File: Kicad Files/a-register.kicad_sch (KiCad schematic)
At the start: 20 parts

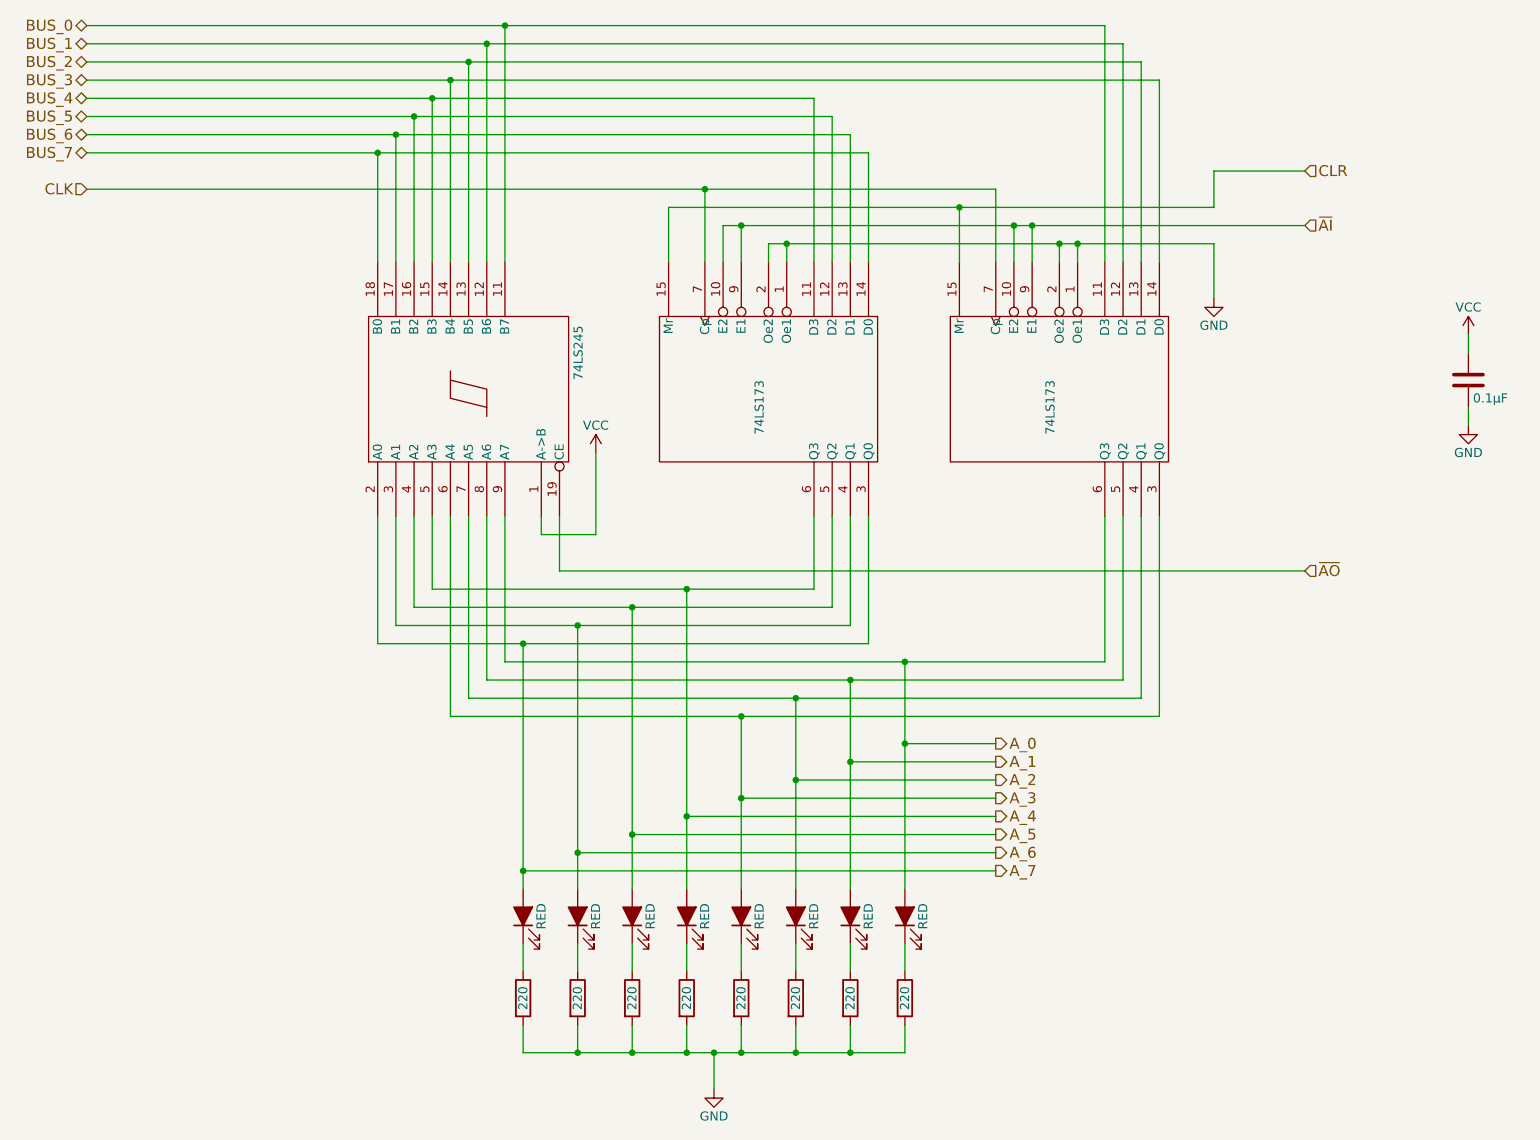
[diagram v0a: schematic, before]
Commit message: started tidy up in control
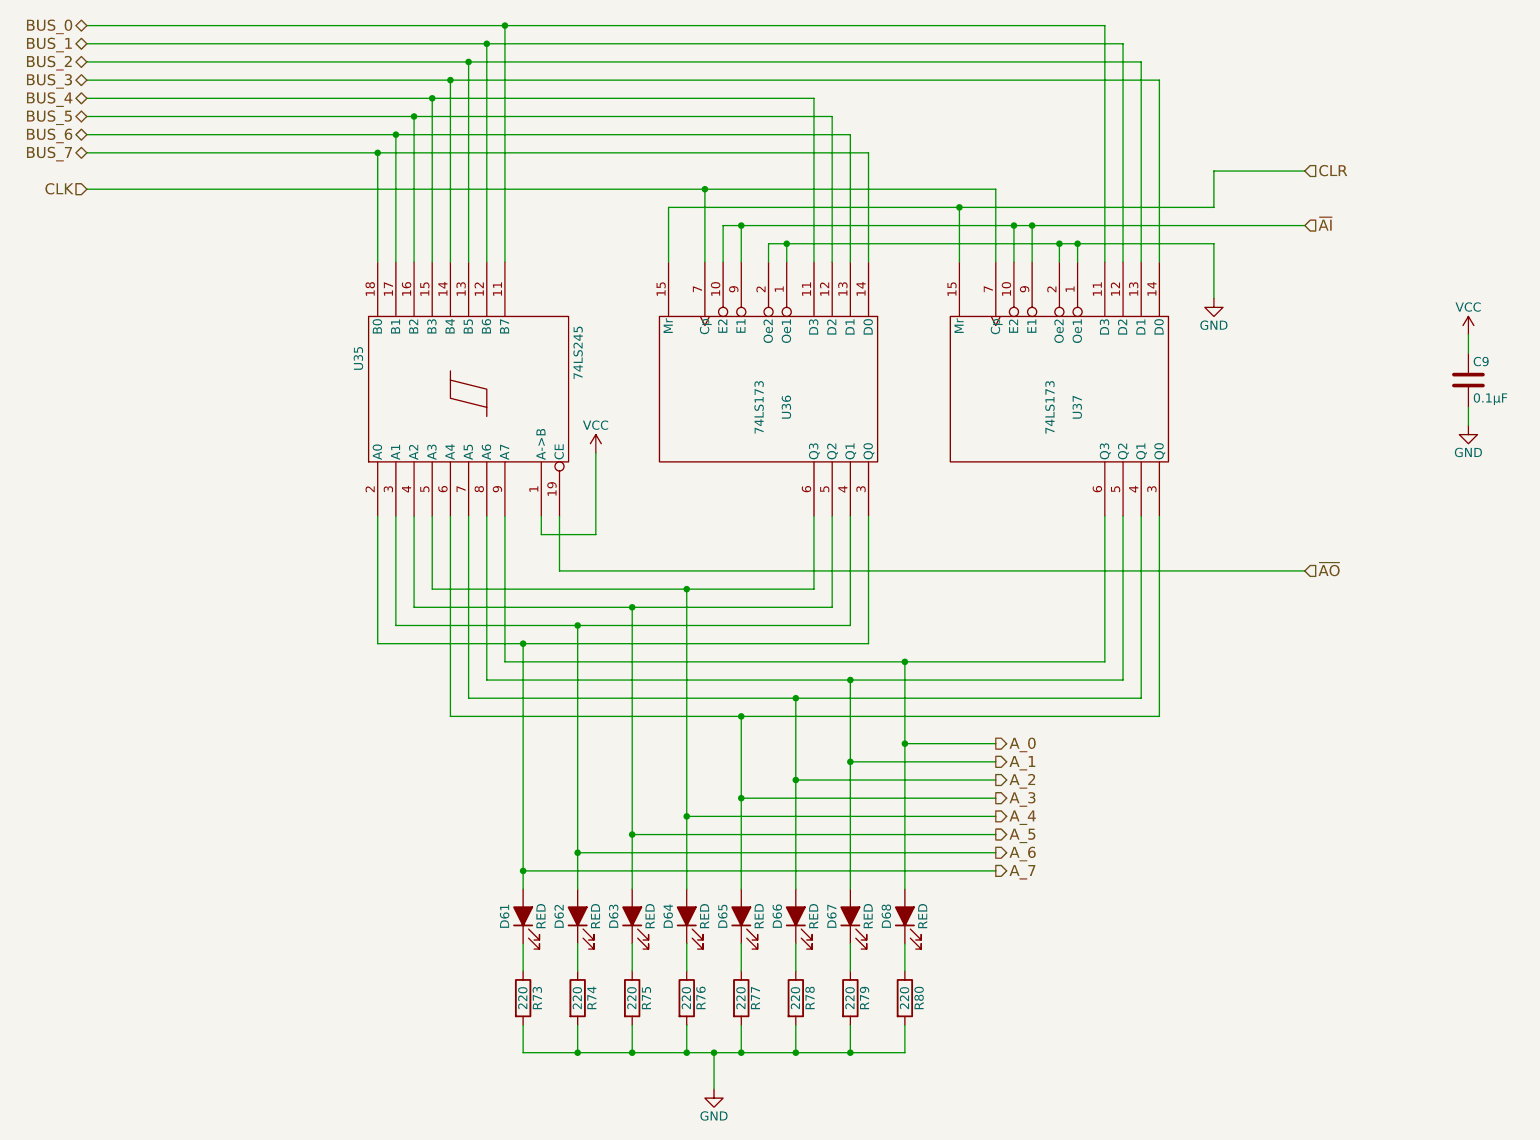
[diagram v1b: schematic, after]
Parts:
- gave numbers to parts that had none: 20
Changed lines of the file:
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@@
   (symbol (lib_id "8bit-computer-rescue:74LS173-8bit-computer-rescue") (at 133.35 68.58 270) (unit 1)
     (in_bom yes) (on_board yes)
-    (property "Reference" "" (id 0) (at 135.89 71.12 0))
+    (property "Reference" "U36" (id 0) (at 135.89 71.12 0))
     (property "Value" "74LS173" (id 1) (at 132.08 71.12 0))
     (property "Footprint" "Package_DIP:DIP-16_W7.62mm" (id 2) (at 133.35 68.58 0)
@@
   (symbol (lib_id "8bit-computer-rescue:LED_ALT-Device") (at 114.3 142.24 90) (unit 1)
     (in_bom yes) (on_board yes)
-    (property "Reference" "" (id 0) (at 111.76 142.24 0))
+    (property "Reference" "D63" (id 0) (at 111.76 142.24 0))
     (property "Value" "RED" (id 1) (at 116.84 142.24 0))
     (property "Footprint" "LED_THT:LED_D5.0mm" (id 2) (at 114.3 142.24 0)
@@
   (symbol (lib_id "8bit-computer-rescue:LED_ALT-Device") (at 144.78 142.24 90) (unit 1)
     (in_bom yes) (on_board yes)
-    (property "Reference" "" (id 0) (at 142.24 142.24 0))
+    (property "Reference" "D67" (id 0) (at 142.24 142.24 0))
     (property "Value" "RED" (id 1) (at 147.32 142.24 0))
     (property "Footprint" "LED_THT:LED_D5.0mm" (id 2) (at 144.78 142.24 0)
@@
   (symbol (lib_id "8bit-computer-rescue:LED_ALT-Device") (at 152.4 142.24 90) (unit 1)
     (in_bom yes) (on_board yes)
-    (property "Reference" "" (id 0) (at 149.86 142.24 0))
+    (property "Reference" "D68" (id 0) (at 149.86 142.24 0))
     (property "Value" "RED" (id 1) (at 154.94 142.24 0))
     (property "Footprint" "LED_THT:LED_D5.0mm" (id 2) (at 152.4 142.24 0)
@@
   (symbol (lib_id "Device:R") (at 114.3 153.67 0) (unit 1)
     (in_bom yes) (on_board yes)
-    (property "Reference" "" (id 0) (at 116.332 153.67 90))
+    (property "Reference" "R75" (id 0) (at 116.332 153.67 90))
     (property "Value" "220" (id 1) (at 114.3 153.67 90))
     (property "Footprint" "Resistor_THT:R_Axial_DIN0207_L6.3mm_D2.5mm_P7.62mm_Horizontal" (id 2) (at 112.522 153.67 90)
@@
   (symbol (lib_id "Device:R") (at 121.92 153.67 0) (unit 1)
     (in_bom yes) (on_board yes)
-    (property "Reference" "" (id 0) (at 123.952 153.67 90))
+    (property "Reference" "R76" (id 0) (at 123.952 153.67 90))
     (property "Value" "220" (id 1) (at 121.92 153.67 90))
     (property "Footprint" "Resistor_THT:R_Axial_DIN0207_L6.3mm_D2.5mm_P7.62mm_Horizontal" (id 2) (at 120.142 153.67 90)
@@
   (symbol (lib_id "Device:R") (at 137.16 153.67 0) (unit 1)
     (in_bom yes) (on_board yes)
-    (property "Reference" "" (id 0) (at 139.192 153.67 90))
+    (property "Reference" "R78" (id 0) (at 139.192 153.67 90))
     (property "Value" "220" (id 1) (at 137.16 153.67 90))
     (property "Footprint" "Resistor_THT:R_Axial_DIN0207_L6.3mm_D2.5mm_P7.62mm_Horizontal" (id 2) (at 135.382 153.67 90)
@@
   (symbol (lib_id "Device:R") (at 152.4 153.67 0) (unit 1)
     (in_bom yes) (on_board yes)
-    (property "Reference" "" (id 0) (at 154.432 153.67 90))
+    (property "Reference" "R80" (id 0) (at 154.432 153.67 90))
     (property "Value" "220" (id 1) (at 152.4 153.67 90))
     (property "Footprint" "Resistor_THT:R_Axial_DIN0207_L6.3mm_D2.5mm_P7.62mm_Horizontal" (id 2) (at 150.622 153.67 90)
@@
   (symbol (lib_id "8bit-computer-rescue:74LS173-8bit-computer-rescue") (at 173.99 68.58 270) (unit 1)
     (in_bom yes) (on_board yes)
-    (property "Reference" "" (id 0) (at 176.53 71.12 0))
+    (property "Reference" "U37" (id 0) (at 176.53 71.12 0))
     (property "Value" "74LS173" (id 1) (at 172.72 71.12 0))
     (property "Footprint" "Package_DIP:DIP-16_W7.62mm" (id 2) (at 173.99 68.58 0)
@@
   (symbol (lib_id "8bit-computer-rescue:74LS245-8bit-computer-rescue") (at 91.44 68.58 90) (unit 1)
     (in_bom yes) (on_board yes)
-    (property "Reference" "" (id 0) (at 76.835 66.04 0)
+    (property "Reference" "U35" (id 0) (at 76.835 66.04 0)
       (effects (font (size 1.27 1.27)) (justify left bottom))
     )
@@
   (symbol (lib_id "8bit-computer-rescue:LED_ALT-Device") (at 99.06 142.24 90) (unit 1)
     (in_bom yes) (on_board yes)
-    (property "Reference" "" (id 0) (at 96.52 142.24 0))
+    (property "Reference" "D61" (id 0) (at 96.52 142.24 0))
     (property "Value" "RED" (id 1) (at 101.6 142.24 0))
     (property "Footprint" "LED_THT:LED_D5.0mm" (id 2) (at 99.06 142.24 0)
@@
   (symbol (lib_id "8bit-computer-rescue:LED_ALT-Device") (at 106.68 142.24 90) (unit 1)
     (in_bom yes) (on_board yes)
-    (property "Reference" "" (id 0) (at 104.14 142.24 0))
+    (property "Reference" "D62" (id 0) (at 104.14 142.24 0))
     (property "Value" "RED" (id 1) (at 109.22 142.24 0))
     (property "Footprint" "LED_THT:LED_D5.0mm" (id 2) (at 106.68 142.24 0)
@@
   (symbol (lib_id "8bit-computer-rescue:LED_ALT-Device") (at 121.92 142.24 90) (unit 1)
     (in_bom yes) (on_board yes)
-    (property "Reference" "" (id 0) (at 119.38 142.24 0))
+    (property "Reference" "D64" (id 0) (at 119.38 142.24 0))
     (property "Value" "RED" (id 1) (at 124.46 142.24 0))
     (property "Footprint" "LED_THT:LED_D5.0mm" (id 2) (at 121.92 142.24 0)
@@
   (symbol (lib_id "8bit-computer-rescue:LED_ALT-Device") (at 129.54 142.24 90) (unit 1)
     (in_bom yes) (on_board yes)
-    (property "Reference" "" (id 0) (at 127 142.24 0))
+    (property "Reference" "D65" (id 0) (at 127 142.24 0))
     (property "Value" "RED" (id 1) (at 132.08 142.24 0))
     (property "Footprint" "LED_THT:LED_D5.0mm" (id 2) (at 129.54 142.24 0)
@@
   (symbol (lib_id "8bit-computer-rescue:LED_ALT-Device") (at 137.16 142.24 90) (unit 1)
     (in_bom yes) (on_board yes)
-    (property "Reference" "" (id 0) (at 134.62 142.24 0))
+    (property "Reference" "D66" (id 0) (at 134.62 142.24 0))
     (property "Value" "RED" (id 1) (at 139.7 142.24 0))
     (property "Footprint" "LED_THT:LED_D5.0mm" (id 2) (at 137.16 142.24 0)
@@
   (symbol (lib_id "Device:R") (at 99.06 153.67 0) (unit 1)
     (in_bom yes) (on_board yes)
-    (property "Reference" "" (id 0) (at 101.092 153.67 90))
+    (property "Reference" "R73" (id 0) (at 101.092 153.67 90))
     (property "Value" "220" (id 1) (at 99.06 153.67 90))
     (property "Footprint" "Resistor_THT:R_Axial_DIN0207_L6.3mm_D2.5mm_P7.62mm_Horizontal" (id 2) (at 97.282 153.67 90)
@@
   (symbol (lib_id "Device:R") (at 106.68 153.67 0) (unit 1)
     (in_bom yes) (on_board yes)
-    (property "Reference" "" (id 0) (at 108.712 153.67 90))
+    (property "Reference" "R74" (id 0) (at 108.712 153.67 90))
     (property "Value" "220" (id 1) (at 106.68 153.67 90))
     (property "Footprint" "Resistor_THT:R_Axial_DIN0207_L6.3mm_D2.5mm_P7.62mm_Horizontal" (id 2) (at 104.902 153.67 90)
@@
   (symbol (lib_id "Device:R") (at 129.54 153.67 0) (unit 1)
     (in_bom yes) (on_board yes)
-    (property "Reference" "" (id 0) (at 131.572 153.67 90))
+    (property "Reference" "R77" (id 0) (at 131.572 153.67 90))
     (property "Value" "220" (id 1) (at 129.54 153.67 90))
     (property "Footprint" "Resistor_THT:R_Axial_DIN0207_L6.3mm_D2.5mm_P7.62mm_Horizontal" (id 2) (at 127.762 153.67 90)
@@
   (symbol (lib_id "Device:R") (at 144.78 153.67 0) (unit 1)
     (in_bom yes) (on_board yes)
-    (property "Reference" "" (id 0) (at 146.812 153.67 90))
+    (property "Reference" "R79" (id 0) (at 146.812 153.67 90))
     (property "Value" "220" (id 1) (at 144.78 153.67 90))
     (property "Footprint" "Resistor_THT:R_Axial_DIN0207_L6.3mm_D2.5mm_P7.62mm_Horizontal" (id 2) (at 143.002 153.67 90)
@@
   (symbol (lib_id "Device:C") (at 231.14 67.31 0) (unit 1)
     (in_bom yes) (on_board yes)
-    (property "Reference" "" (id 0) (at 231.775 64.77 0)
+    (property "Reference" "C9" (id 0) (at 231.775 64.77 0)
       (effects (font (size 1.27 1.27)) (justify left))
     )

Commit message: work on cl
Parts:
- C19: renamed from C9; value 0.1µF -> C
- R77: renamed from R73; value 220 -> R
- R78: renamed from R74; value 220 -> R
- R79: renamed from R75; value 220 -> R
- R80: renamed from R76; value 220 -> R
- R81: renamed from R77; value 220 -> R
- R82: renamed from R78; value 220 -> R
- R83: renamed from R79; value 220 -> R
- R84: renamed from R80; value 220 -> R
- renumbered D61 to D42, D62 to D43, D63 to D44, D64 to D45, D65 to D46, D66 to D47, D67 to D48, D68 to D49, U35 to U36, U36 to U37, U37 to U38

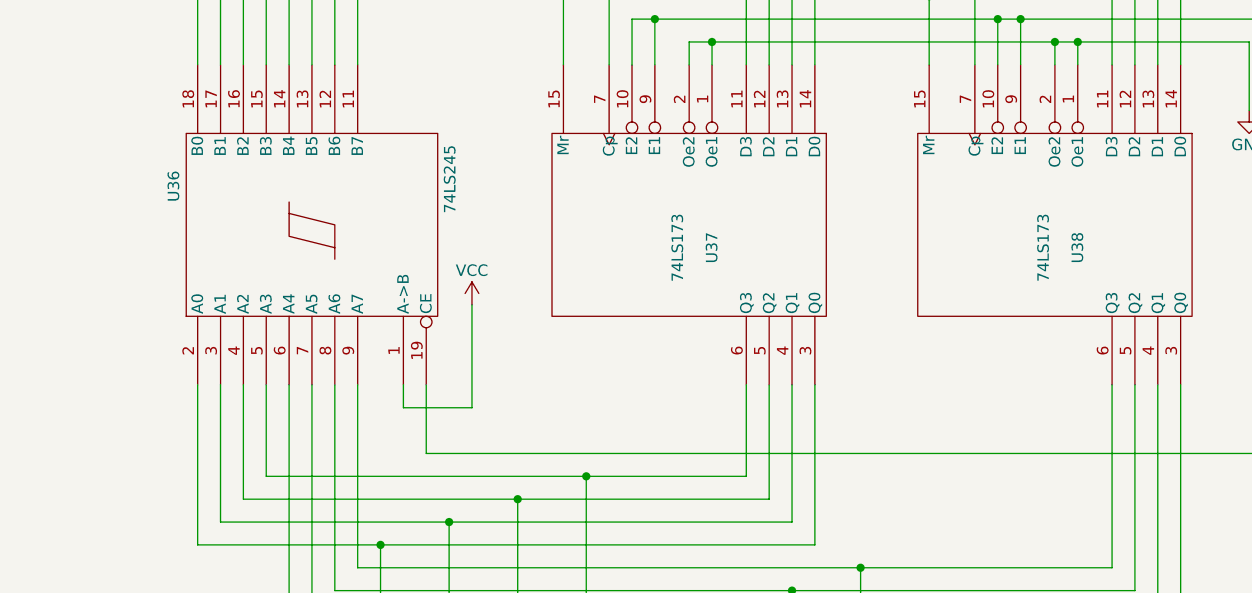
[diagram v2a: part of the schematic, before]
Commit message: fixed ecc problems
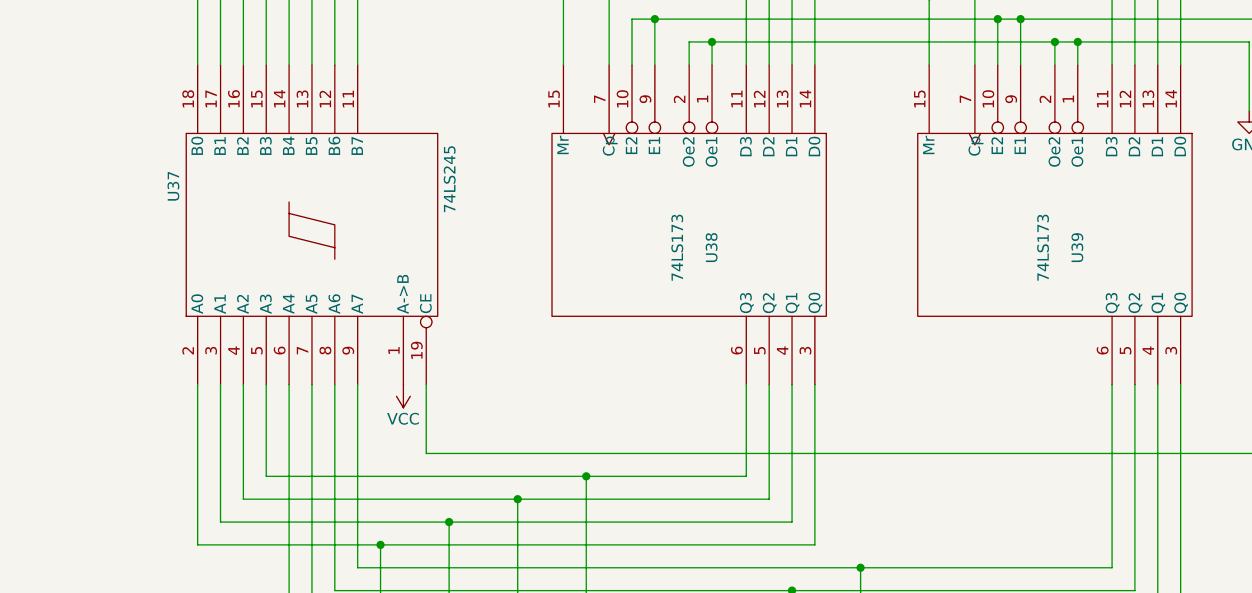
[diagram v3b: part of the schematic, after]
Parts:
- renumbered U36 to U37, U37 to U38, U38 to U39
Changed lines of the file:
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@@
-    (stroke (width 0) (type default) (color 0 0 0 0))
-  )
-  (wire (pts (xy 101.6 88.9) (xy 109.22 88.9))
     (stroke (width 0) (type default) (color 0 0 0 0))
   )
@@
     (stroke (width 0) (type default) (color 0 0 0 0))
   )
-  (wire (pts (xy 109.22 88.9) (xy 109.22 77.47))
-    (stroke (width 0) (type default) (color 0 0 0 0))
-  )
   (wire (pts (xy 165.1 133.35) (xy 106.68 133.35))
     (stroke (width 0) (type default) (color 0 0 0 0))
@@
     (stroke (width 0) (type default) (color 0 0 0 0))
   )
-  (wire (pts (xy 101.6 86.36) (xy 101.6 88.9))
-    (stroke (width 0) (type default) (color 0 0 0 0))
-  )
   (wire (pts (xy 121.92 128.27) (xy 165.1 128.27))
     (stroke (width 0) (type default) (color 0 0 0 0))
@@
   (symbol (lib_id "8bit-computer-rescue:74LS173-8bit-computer-rescue") (at 133.35 68.58 270) (unit 1)
     (in_bom yes) (on_board yes)
-    (property "Reference" "U37" (id 0) (at 135.89 71.12 0))
+    (property "Reference" "U38" (id 0) (at 135.89 71.12 0))
     (property "Value" "74LS173" (id 1) (at 132.08 71.12 0))
     (property "Footprint" "Package_DIP:DIP-16_W7.62mm" (id 2) (at 133.35 68.58 0)
@@
     (pin "2")
   )
-  (symbol (lib_id "power:VCC") (at 109.22 77.47 0) (unit 1)
-    (in_bom yes) (on_board yes)
-    (property "Reference" "#PWR0112" (id 0) (at 109.22 81.28 0)
-      (effects (font (size 1.27 1.27)) hide)
-    )
-    (property "Value" "VCC" (id 1) (at 109.22 73.66 0))
-    (property "Footprint" "" (id 2) (at 109.22 77.47 0)
-      (effects (font (size 1.27 1.27)) hide)
-    )
-    (property "Datasheet" "" (id 3) (at 109.22 77.47 0)
+  (symbol (lib_id "power:VCC") (at 101.6 86.36 180) (unit 1)
+    (in_bom yes) (on_board yes)
+    (property "Reference" "#PWR0116" (id 0) (at 101.6 82.55 0)
+      (effects (font (size 1.27 1.27)) hide)
+    )
+    (property "Value" "VCC" (id 1) (at 101.6 90.17 0))
+    (property "Footprint" "" (id 2) (at 101.6 86.36 0)
+      (effects (font (size 1.27 1.27)) hide)
+    )
+    (property "Datasheet" "" (id 3) (at 101.6 86.36 0)
       (effects (font (size 1.27 1.27)) hide)
     )
@@
   (symbol (lib_id "8bit-computer-rescue:74LS173-8bit-computer-rescue") (at 173.99 68.58 270) (unit 1)
     (in_bom yes) (on_board yes)
-    (property "Reference" "U38" (id 0) (at 176.53 71.12 0))
+    (property "Reference" "U39" (id 0) (at 176.53 71.12 0))
     (property "Value" "74LS173" (id 1) (at 172.72 71.12 0))
     (property "Footprint" "Package_DIP:DIP-16_W7.62mm" (id 2) (at 173.99 68.58 0)
@@
   (symbol (lib_id "8bit-computer-rescue:74LS245-8bit-computer-rescue") (at 91.44 68.58 90) (unit 1)
     (in_bom yes) (on_board yes)
-    (property "Reference" "U36" (id 0) (at 76.835 66.04 0)
+    (property "Reference" "U37" (id 0) (at 76.835 66.04 0)
       (effects (font (size 1.27 1.27)) (justify left bottom))
     )
@@
   (symbol (lib_id "power:GND") (at 125.73 166.37 0) (unit 1)
     (in_bom yes) (on_board yes)
-    (property "Reference" "#PWR0113" (id 0) (at 125.73 172.72 0)
+    (property "Reference" "#PWR0117" (id 0) (at 125.73 172.72 0)
       (effects (font (size 1.27 1.27)) hide)
     )
@@
   (symbol (lib_id "power:GND") (at 195.58 55.88 0) (unit 1)
     (in_bom yes) (on_board yes)
-    (property "Reference" "#PWR0114" (id 0) (at 195.58 62.23 0)
+    (property "Reference" "#PWR0118" (id 0) (at 195.58 62.23 0)
       (effects (font (size 1.27 1.27)) hide)
     )
@@
   (symbol (lib_id "power:GND") (at 231.14 73.66 0) (unit 1)
     (in_bom yes) (on_board yes)
-    (property "Reference" "#PWR0116" (id 0) (at 231.14 80.01 0)
+    (property "Reference" "#PWR0120" (id 0) (at 231.14 80.01 0)
       (effects (font (size 1.27 1.27)) hide)
     )
@@
   (symbol (lib_id "power:VCC") (at 231.14 60.96 0) (unit 1)
     (in_bom yes) (on_board yes)
-    (property "Reference" "#PWR0115" (id 0) (at 231.14 64.77 0)
-      (effects (font (size 1.27 1.27)) hide)
-    )
+    (property "Reference" "#PWR0119" (id 0) (at 231.14 64.77 0)
+      (effects (font (size 1.27 1.27)) hide)
+    )
